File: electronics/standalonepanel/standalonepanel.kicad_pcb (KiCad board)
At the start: 2 copper layers, 135 x 54 mm, 96 parts, among them J1 LEDPWR, J2 USB_C-PD, J3 Speaker, J4 Conn_01x07_Pin, SW1 UP, SW2 BOOT, SW3 SET, SW4 DOWN, SW5 TST-ICE40, SW6 RESET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

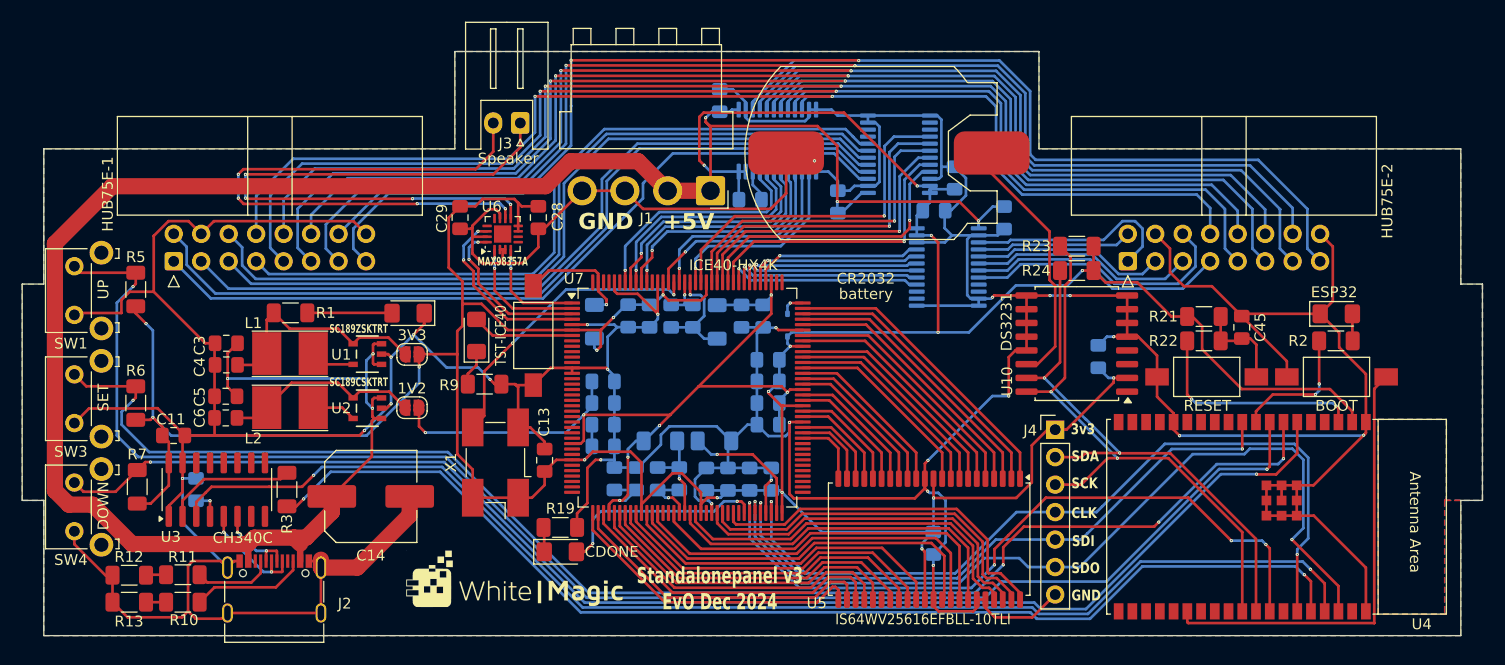
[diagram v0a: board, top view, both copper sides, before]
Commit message: cleanup kicad files and added overview documentation
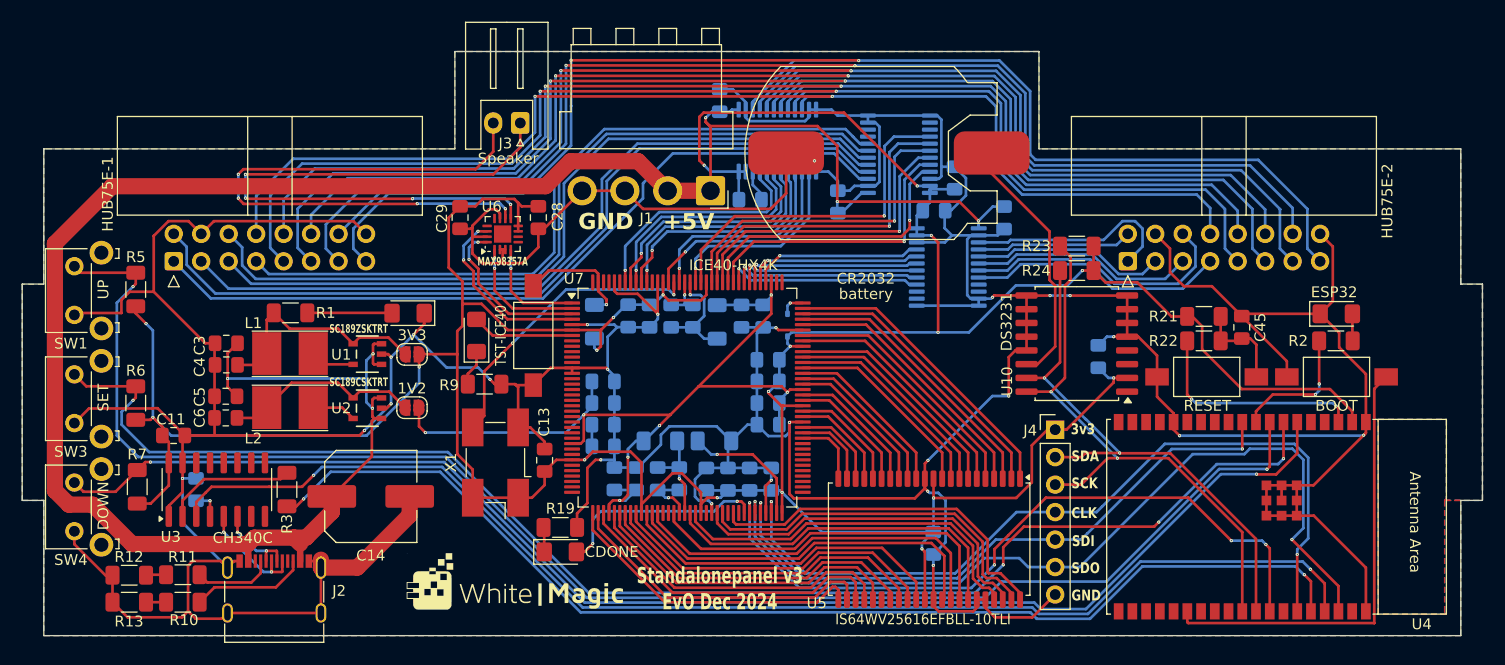
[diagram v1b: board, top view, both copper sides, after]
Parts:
- removed the G*** at (89.5, 138.8)
- added G***: LOGO, 0_whitemagic:white_magic_20mm, F.Cu at (89.5, 139.0)
- J2: value USB_C-PD -> USB_C; footprint 0_whitemagic:USB_C_Receptacle_G-Switch_GT-USB-7010ASV -> 0_whitemagic:USB_C_Receptacle _12pins
